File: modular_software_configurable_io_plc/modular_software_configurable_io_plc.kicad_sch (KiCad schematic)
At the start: 28 parts, among them J1 FW-14-03-G-D-085-155, J10 CLP-108-02-G-D-BE, J11 CLP-102-02-G-D-BE, J12 CLP-102-02-G-D-BE, J13 CLP-102-02-G-D-BE, J14 CLP-108-02-G-D-BE, J15 FW-14-03-G-D-085-155, J16 FW-02-03-G-D-085-155, J17 FW-02-03-G-D-085-155, J18 FW-02-03-G-D-085-155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

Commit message: backup
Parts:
- MOD4: 3dviewer Link (none) -> https://3dviewer.net/index.html#model=https://github.com/io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
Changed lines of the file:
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@@
+			)
+		)
+		(property "3dviewer Link" "https://3dviewer.net/index.html#model=https://github.com/ionutms/KiCAD_Symbols_Generator/blob/main/3D_models/minimal_adin1110.wrl"
+			(at 240.03 49.53 0)
+			(effects
+				(font
+					(size 1.27 1.27)
+				)
+				(justify left)
+				(hide yes)
 			)
 		)

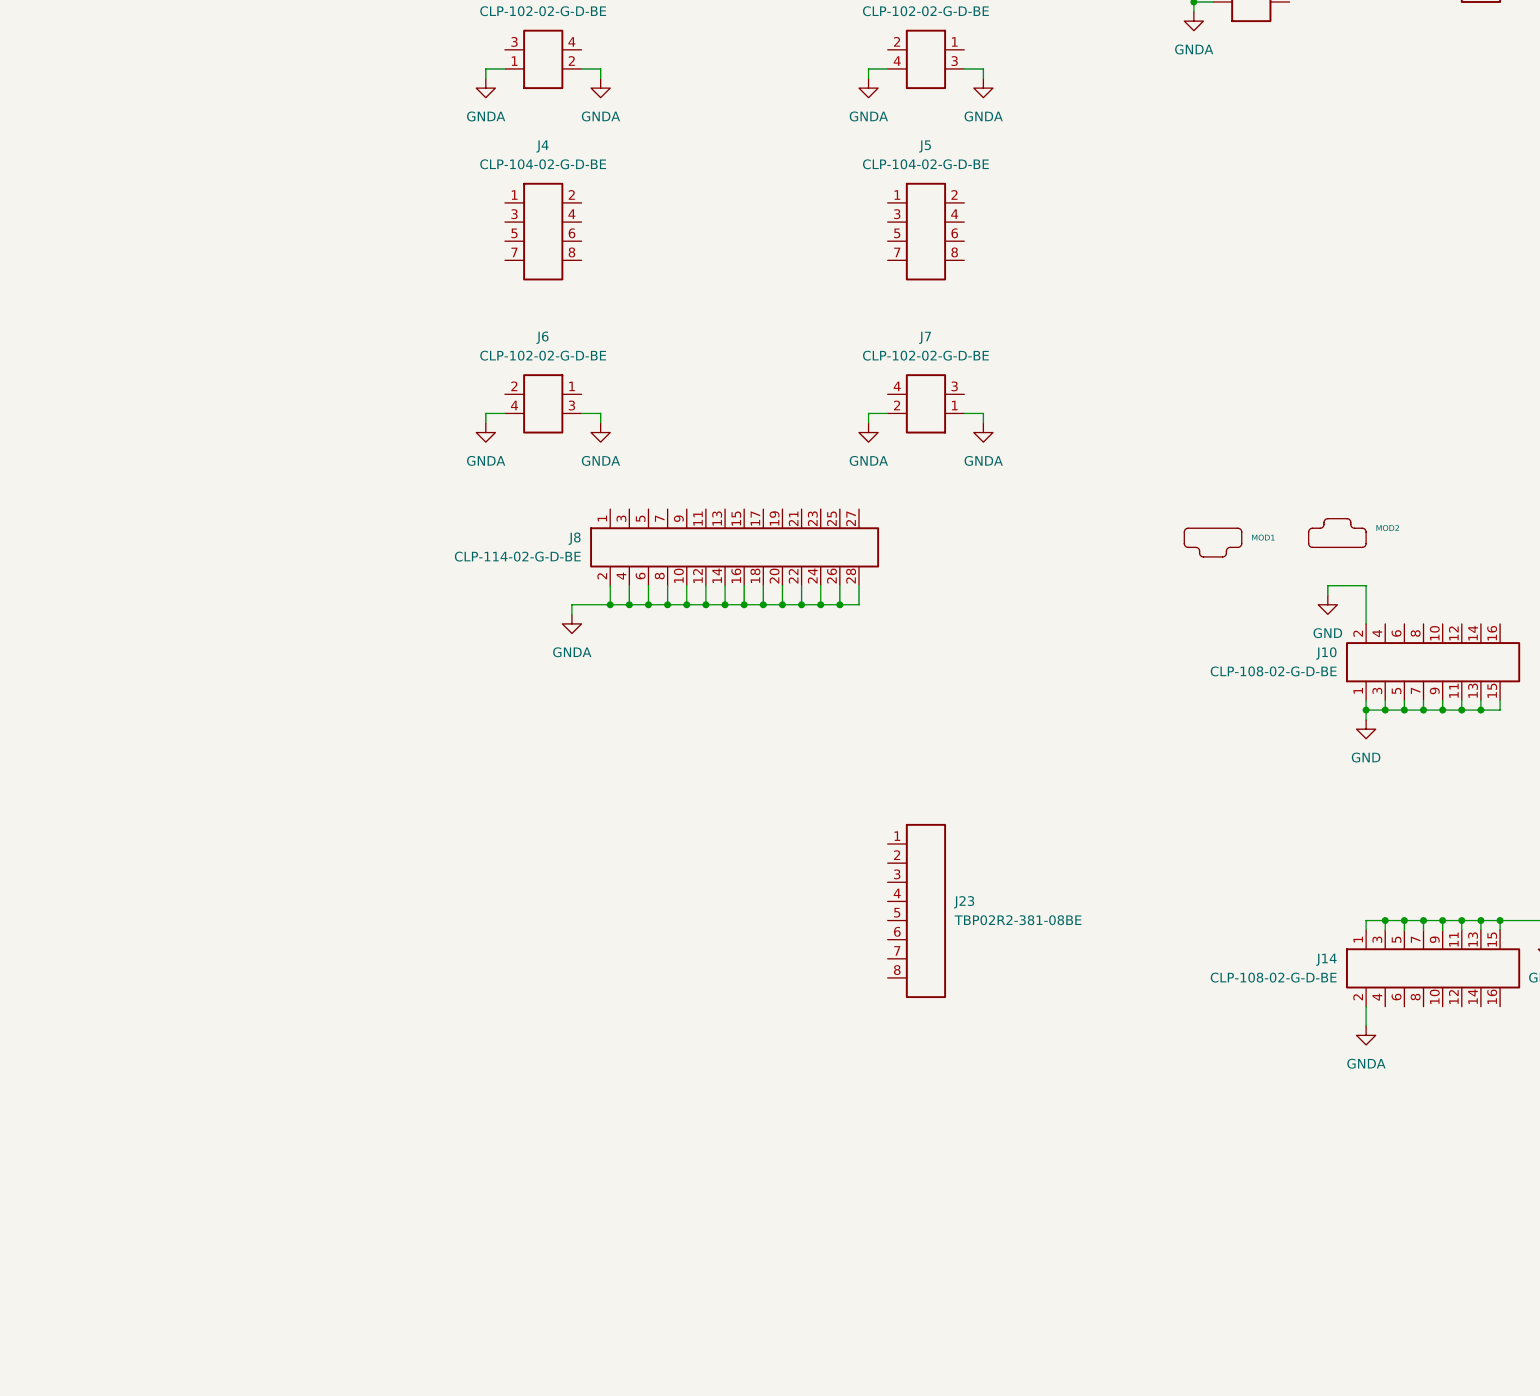
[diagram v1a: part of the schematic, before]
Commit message: Update KiCAD Symbol Generator submodule to latest commit
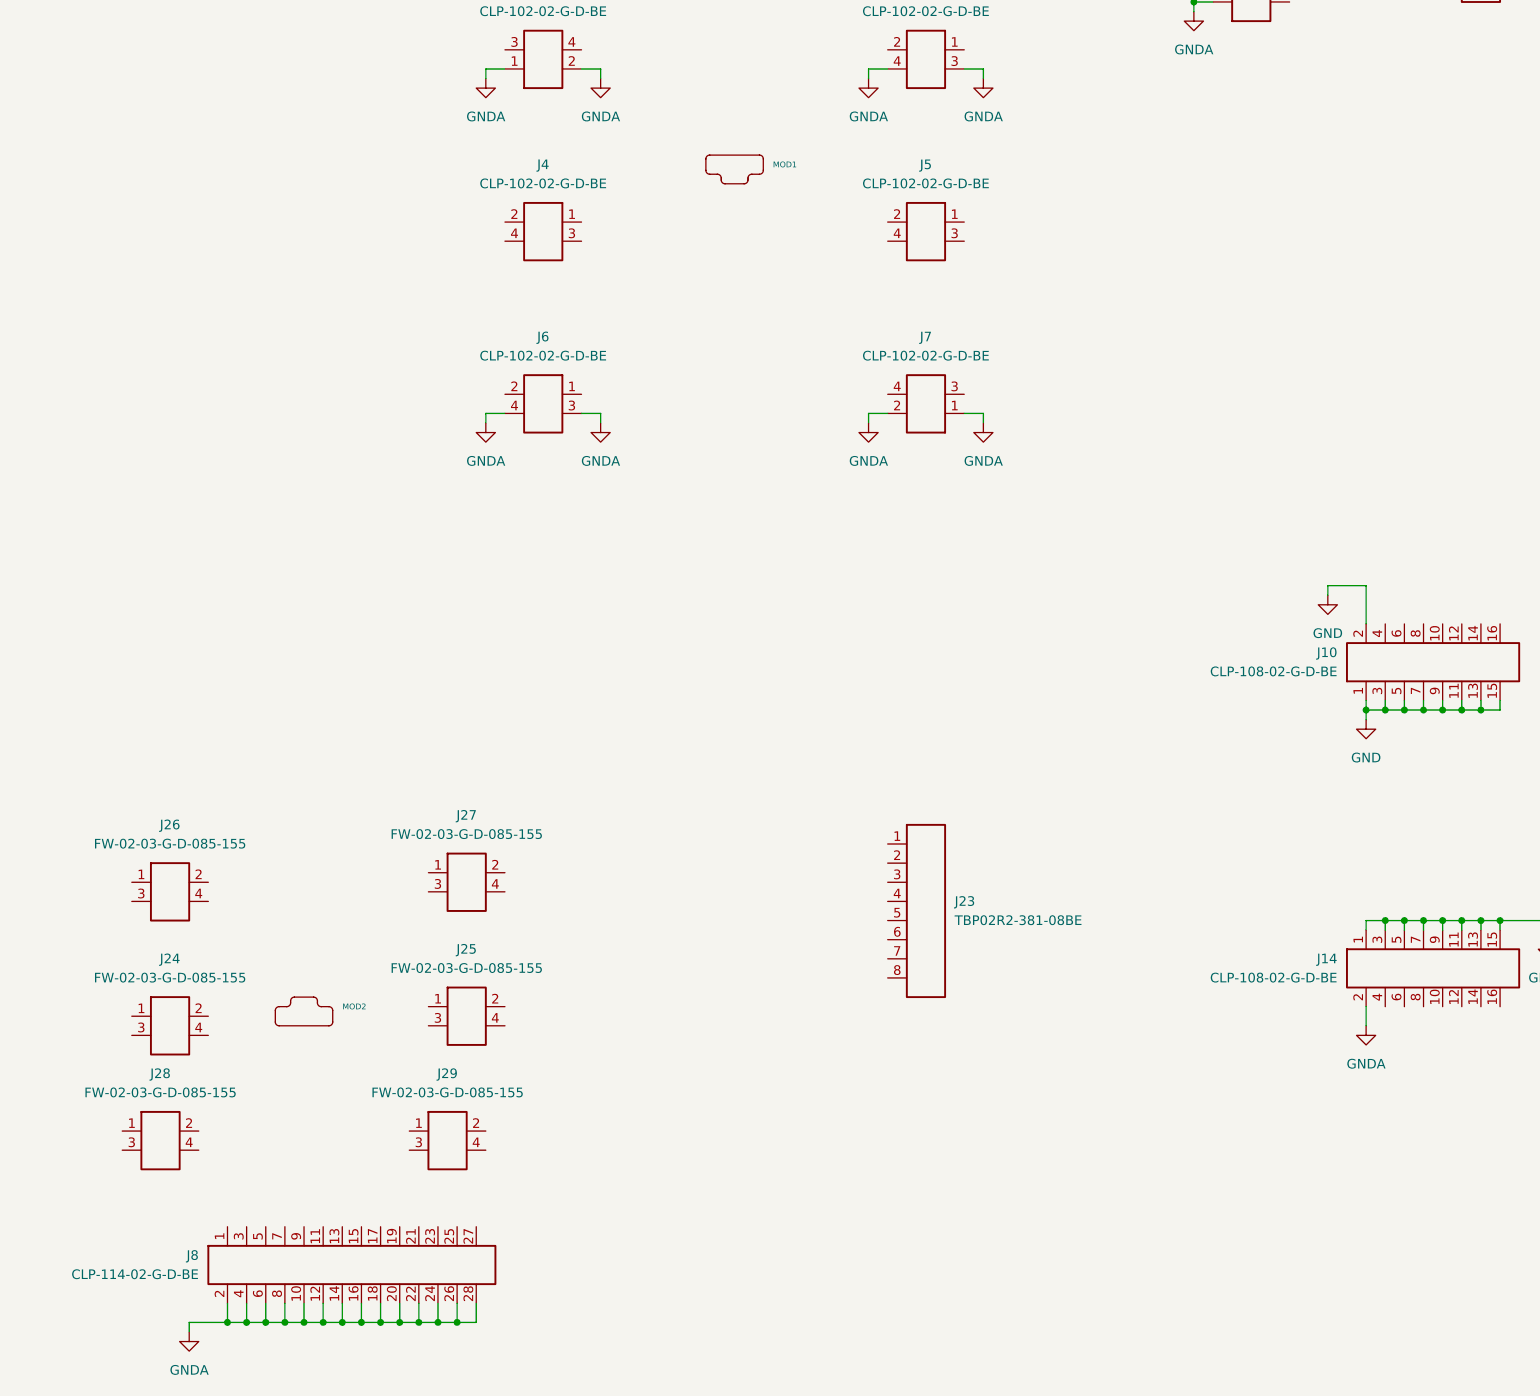
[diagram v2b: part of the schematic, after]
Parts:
- removed J4, J5: CLP-104-02-G-D-BE, connector_footprints:CLP-104-02-G-D-BE, symbol UNITED_CONNECTORS_DATA_BASE:J_CLP-104-02-G-D-BE
- added J24, J25, J26, J27, J28, J29: FW-02-03-G-D-085-155, connector_footprints:FW-02-03-G-D-085-155, symbol UNITED_CONNECTORS_DATA_BASE:J_FW-02-03-G-D-085-155
- added J4, J5: CLP-102-02-G-D-BE, connector_footprints:CLP-102-02-G-D-BE, symbol UNITED_CONNECTORS_DATA_BASE:J_CLP-102-02-G-D-BE
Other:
- moved on the sheet: J8, MOD1, MOD2

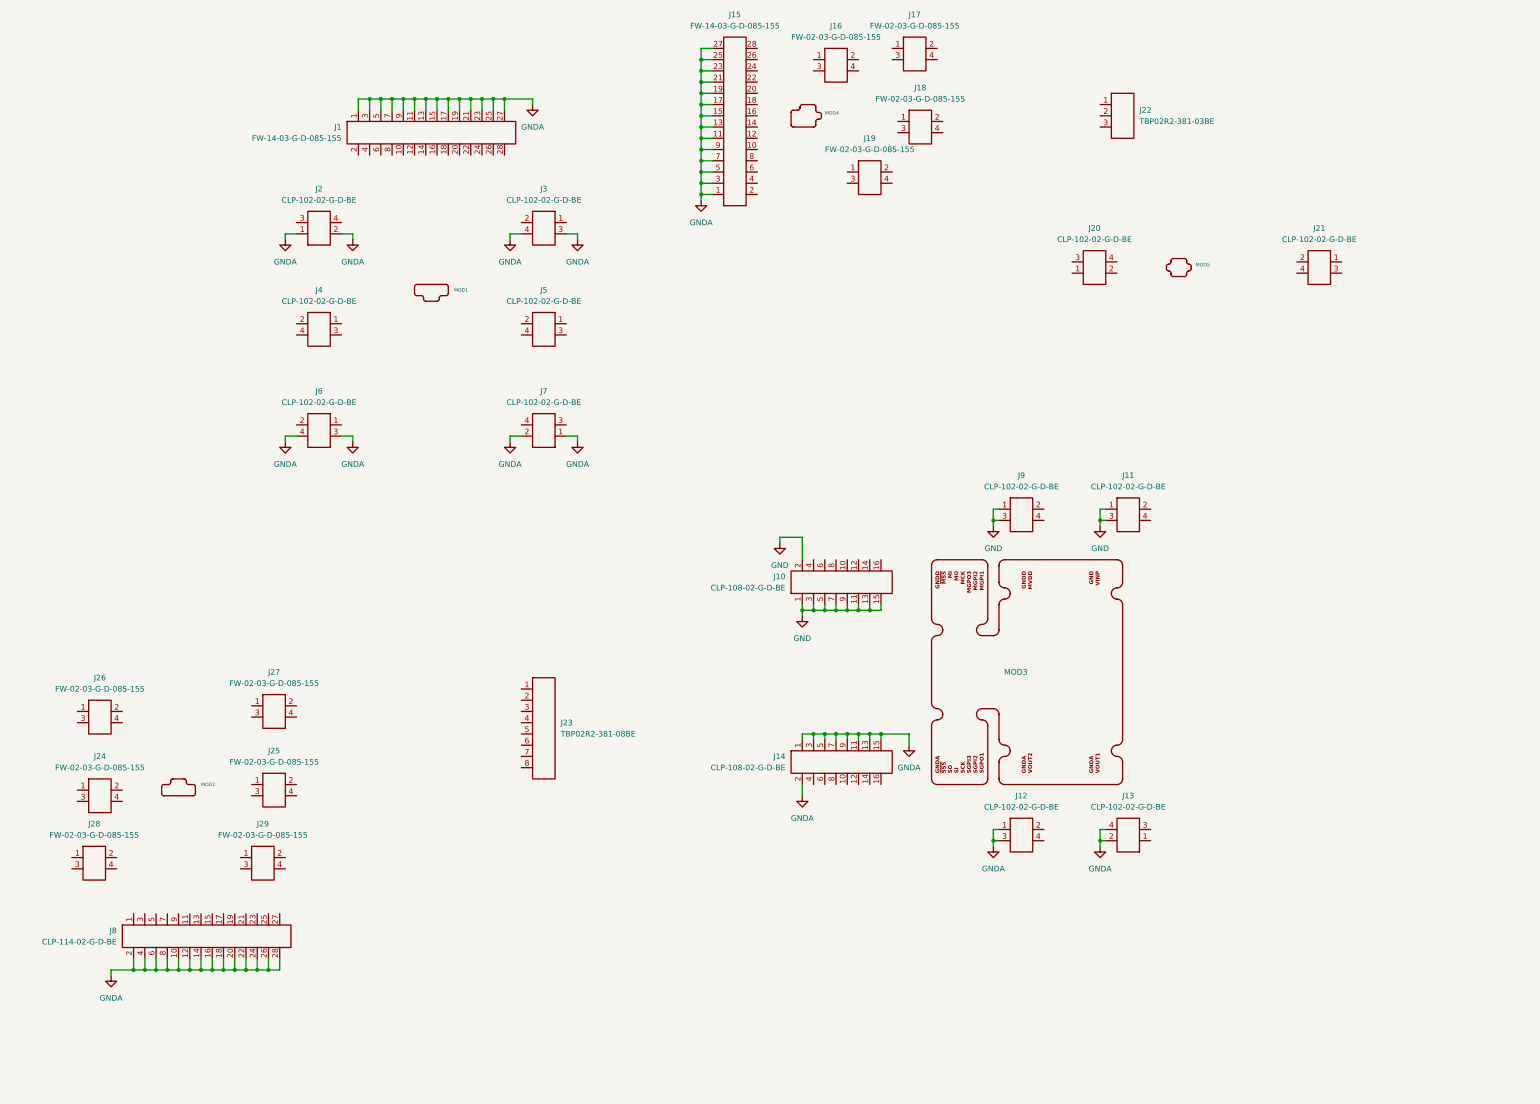
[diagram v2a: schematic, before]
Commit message: Update KiCAD Symbol Generator submodule to latest commit
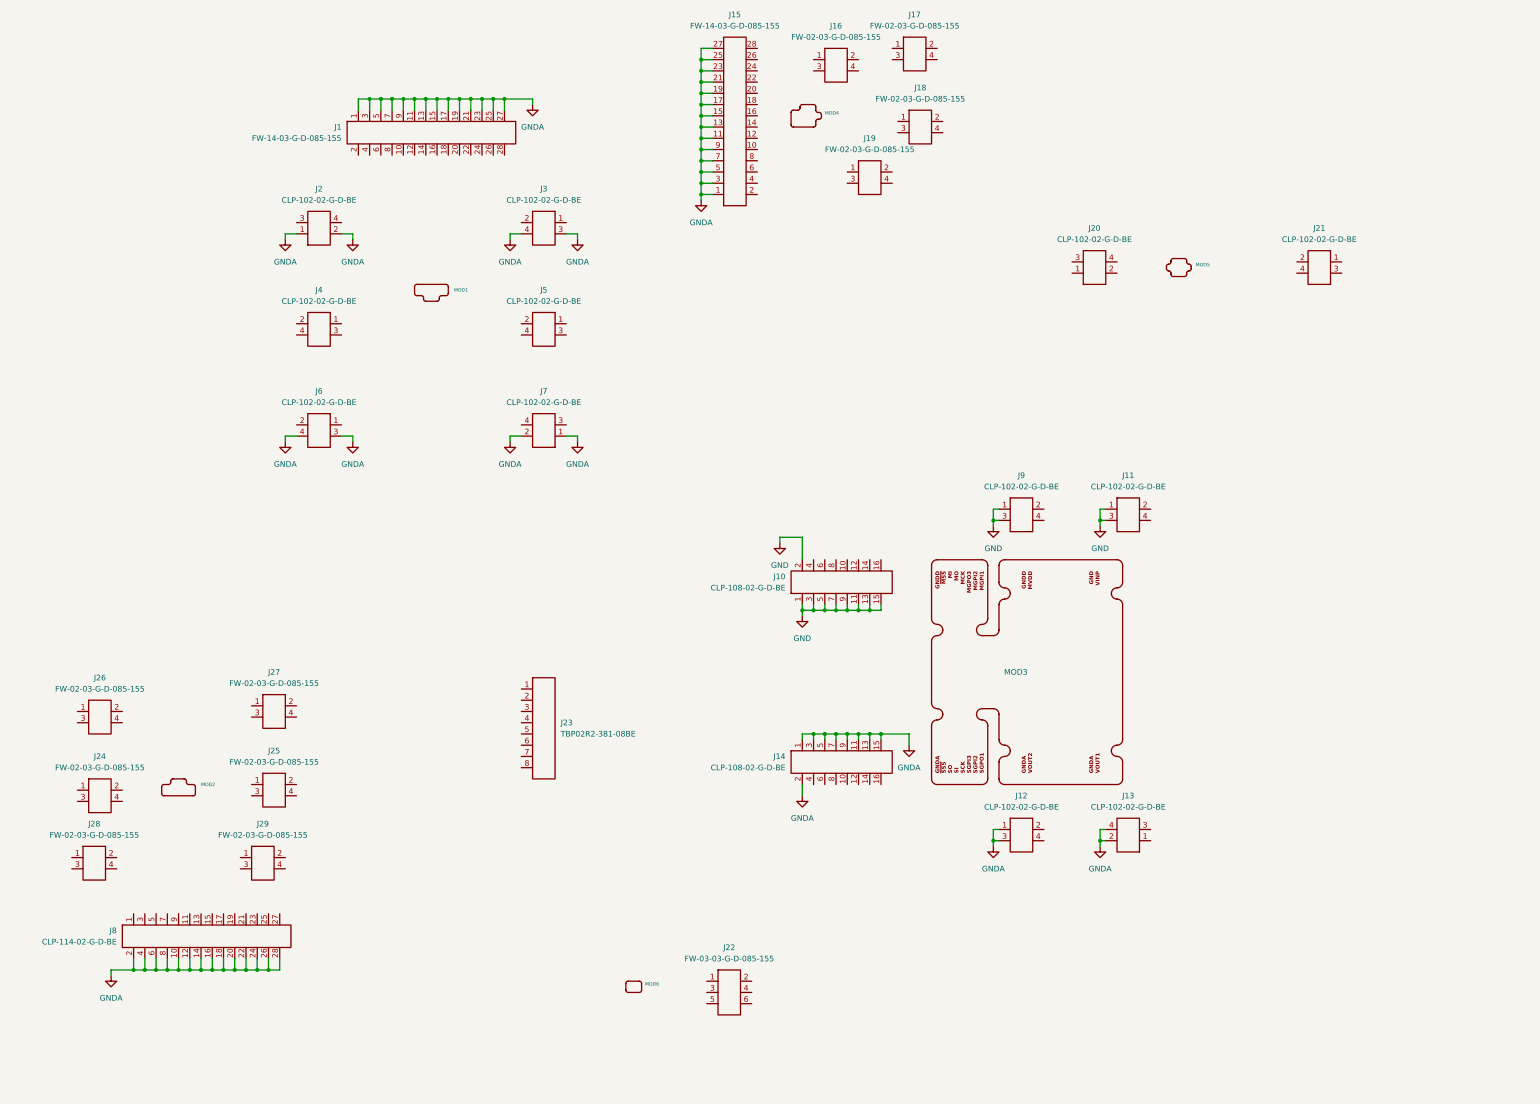
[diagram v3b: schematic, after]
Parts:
- removed J22: TBP02R2-381-03BE, connector_footprints:TBP02R2-381-03BE, symbol UNITED_CONNECTORS_DATA_BASE:J_TBP02R2-381-03BE
- added J22: FW-03-03-G-D-085-155, connector_footprints:FW-03-03-G-D-085-155, symbol UNITED_CONNECTORS_DATA_BASE:J_FW-03-03-G-D-085-155
- added MOD6: ~, modules_footprints:minimal_spoe_hybrid, symbol UNITED_MODULES_DATA_BASE:MINIMAL_SPOE_HYBRID

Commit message: Backup
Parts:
- J21: footprint connector_footprints:CLP-102-02-G-D-BE -> connector_footprints:CLP-103-02-G-D-BE; symbol UNITED_CONNECTORS_DATA_BASE:J_CLP-102-02-G-D-BE -> UNITED_CONNECTORS_DATA_BASE:J_CLP-103-02-G-D-BE; MPN CLP-102-02-G-D-BE -> CLP-103-02-G-D-BE; Mounting Style Through Hole -> Surface Mount; Pin Count 2 -> 3; Symbol Name J_CLP-102-02-G-D-BE -> J_CLP-103-02-G-D-BE; Trustedparts Search https://www.trustedparts.com/en/search/CLP-102-02-G-D-BE -> https://www.trustedparts.com/en/search/CLP-103-02-G-D-BE
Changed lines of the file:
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@@
 	)
 	(symbol
-		(lib_id "UNITED_CONNECTORS_DATA_BASE:J_CLP-102-02-G-D-BE")
+		(lib_id "UNITED_CONNECTORS_DATA_BASE:J_CLP-103-02-G-D-BE")
 		(at 353.06 76.2 0)
 		(mirror y)
@@
 		(fields_autoplaced yes)
 		(property "Reference" "J21"
-			(at 353.06 67.31 0)
+			(at 353.06 66.04 0)
 			(effects
 				(font
@@
 		)
 		(property "Value" "CLP-102-02-G-D-BE"
-			(at 353.06 69.85 0)
-			(effects
-				(font
-					(size 1.27 1.27)
-				)
-			)
-		)
-		(property "Footprint" "connector_footprints:CLP-102-02-G-D-BE"
-			(at 347.98 83.82 0)
+			(at 353.06 68.58 0)
+			(effects
+				(font
+					(size 1.27 1.27)
+				)
+			)
+		)
+		(property "Footprint" "connector_footprints:CLP-103-02-G-D-BE"
+			(at 347.98 85.09 0)
 			(show_name yes)
 			(effects
@@
 		)
 		(property "Datasheet" "https://suddendocs.samtec.com/catalog_english/clp_sm.pdf?_gl=1*1y4jlr9*_gcl_au*MTM0MTYyNTQ5MS4xNzM2MDk5MTUz*_ga*MTYxNDYyMTQ0Mi4xNzM2MDk5MTUz*_ga_3KFNZC07WW*MTczNjY4MDQ4OS4xNS4xLjE3MzY2ODEzNzcuNjAuMC4w"
-			(at 347.98 86.36 0)
-			(show_name yes)
-			(effects
-				(font
-					(size 1.27 1.27)
-				)
-				(justify left)
-				(hide yes)
-			)
-		)
-		(property "Description" "Samtec CLP-1xx-02-G-D-BE series,  2 positions connector,  1.27 mm pitch,  Black,  Vertical mounting,  5.2 A,  300 V,  Through Hole,  Tin plated"
-			(at 347.98 88.9 0)
+			(at 347.98 87.63 0)
+			(show_name yes)
+			(effects
+				(font
+					(size 1.27 1.27)
+				)
+				(justify left)
+				(hide yes)
+			)
+		)
+		(property "Description" "Samtec CLP-1xx-02-G-D-BE series,  3 positions connector,  1.27 mm pitch,  Black,  Vertical mounting,  5.2 A,  300 V,  Surface Mount,  Tin plated"
+			(at 347.98 90.17 0)
 			(show_name yes)
 			(effects
@@
 		)
 		(property "Color" "Black"
-			(at 347.98 91.44 0)
+			(at 347.98 92.71 0)
 			(show_name yes)
 			(effects
@@
 		)
 		(property "Contact Plating" "Tin"
-			(at 347.98 93.98 0)
+			(at 347.98 95.25 0)
 			(show_name yes)
 			(effects
@@
 		)
 		(property "Current Rating (A)" "5.2"
-			(at 347.98 96.52 0)
-			(show_name yes)
-			(effects
-				(font
-					(size 1.27 1.27)
-				)
-				(justify left)
-				(hide yes)
-			)
-		)
-		(property "MPN" "CLP-102-02-G-D-BE"
-			(at 347.98 99.06 0)
+			(at 347.98 97.79 0)
+			(show_name yes)
+			(effects
+				(font
+					(size 1.27 1.27)
+				)
+				(justify left)
+				(hide yes)
+			)
+		)
+		(property "MPN" "CLP-103-02-G-D-BE"
+			(at 347.98 100.33 0)
 			(show_name yes)
 			(effects
@@
 		)
 		(property "Manufacturer" "Samtec"
-			(at 347.98 101.6 0)
+			(at 347.98 102.87 0)
 			(show_name yes)
 			(effects
@@
 		)
 		(property "Mounting Angle" "Vertical"
-			(at 347.98 104.14 0)
-			(show_name yes)
-			(effects
-				(font
-					(size 1.27 1.27)
-				)
-				(justify left)
-				(hide yes)
-			)
-		)
-		(property "Mounting Style" "Through Hole"
-			(at 347.98 106.68 0)
+			(at 347.98 105.41 0)
+			(show_name yes)
+			(effects
+				(font
+					(size 1.27 1.27)
+				)
+				(justify left)
+				(hide yes)
+			)
+		)
+		(property "Mounting Style" "Surface Mount"
+			(at 347.98 107.95 0)
 			(show_name yes)
 			(effects
@@
 		)
 		(property "Number of Rows" "2"
-			(at 347.98 109.22 0)
-			(show_name yes)
-			(effects
-				(font
-					(size 1.27 1.27)
-				)
-				(justify left)
-				(hide yes)
-			)
-		)
-		(property "Pin Count" "2"
-			(at 347.98 111.76 0)
+			(at 347.98 110.49 0)
+			(show_name yes)
+			(effects
+				(font
+					(size 1.27 1.27)
+				)
+				(justify left)
+				(hide yes)
+			)
+		)
+		(property "Pin Count" "3"
+			(at 347.98 113.03 0)
 			(show_name yes)
 			(effects
@@
 		)
 		(property "Pitch (mm)" "1.27"
-			(at 347.98 114.3 0)
+			(at 347.98 115.57 0)
 			(show_name yes)
 			(effects
@@
 		)
 		(property "Series" "CLP-1xx-02-G-D-BE"
-			(at 347.98 116.84 0)
-			(show_name yes)
-			(effects
-				(font
-					(size 1.27 1.27)
-				)
-				(justify left)
-				(hide yes)
-			)
-		)
-		(property "Symbol Name" "J_CLP-102-02-G-D-BE"
-			(at 347.98 119.38 0)
-			(show_name yes)
-			(effects
-				(font
-					(size 1.27 1.27)
-				)
-				(justify left)
-				(hide yes)
-			)
-		)
-		(property "Trustedparts Search" "https://www.trustedparts.com/en/search/CLP-102-02-G-D-BE"
-			(at 347.98 121.92 0)
+			(at 347.98 118.11 0)
+			(show_name yes)
+			(effects
+				(font
+					(size 1.27 1.27)
+				)
+				(justify left)
+				(hide yes)
+			)
+		)
+		(property "Symbol Name" "J_CLP-103-02-G-D-BE"
+			(at 347.98 120.65 0)
+			(show_name yes)
+			(effects
+				(font
+					(size 1.27 1.27)
+				)
+				(justify left)
+				(hide yes)
+			)
+		)
+		(property "Trustedparts Search" "https://www.trustedparts.com/en/search/CLP-103-02-G-D-BE"
+			(at 347.98 123.19 0)
 			(show_name yes)
 			(effects
@@
 		)
 		(property "Voltage Rating (V)" "300"
-			(at 347.98 124.46 0)
+			(at 347.98 125.73 0)
 			(show_name yes)
 			(effects
@@
 		(pin "3"
 		)
+		(pin "6"
+		)
+		(pin "5"
+		)
 		(instances
